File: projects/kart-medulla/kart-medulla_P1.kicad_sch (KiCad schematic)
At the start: 55 parts, among them CN1 1990012, CN10 1990012, CN2 1990012, CN3 1990012, CN4 1990012, CN5 1990012, CN6 1990012, CN7 1990012, CN8 1990012, CN9 1990012, Q3 IRLZ44NPBF, Q4 BSS123_C5184436, U13 MCP4922-E/SL, U14 MAX4660EUA+T, U19 L7805CDT_C20611927, U23 SSW-122-01-T-D, U24 SSW-122-01-T-S, U25 PCF8574T/3,518, U4 LM358DR, U5 SN74LVC3G17DCTR

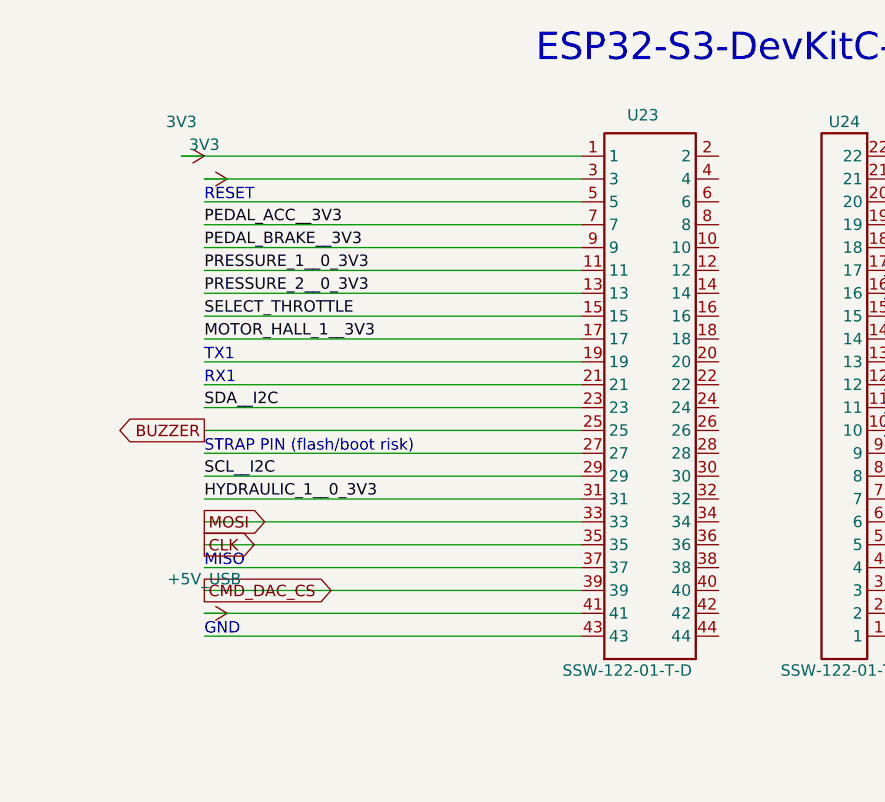
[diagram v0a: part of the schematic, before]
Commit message: kart-medulla: wire ESP32 header pin pairs + add junctions on shared net points
Connect U23 (SSW-122-01-T-D, ESP32 DevKitC double-row header) odd-even
pin pairs 5-6..43-44 horizontally so each row maps to one ESP32 GPIO
visible on both physical rows of the header. Added 22 junction markers
on the left column where label-wires meet the new horizontals (3-way
points need explicit junctions when wires are added programmatically;
KiCad GUI auto-creates them only at draw time). ERC: 111 -> 83.

Co-Authored-By: Claude Opus 4.7 (1M context) <noreply@anthropic.com>
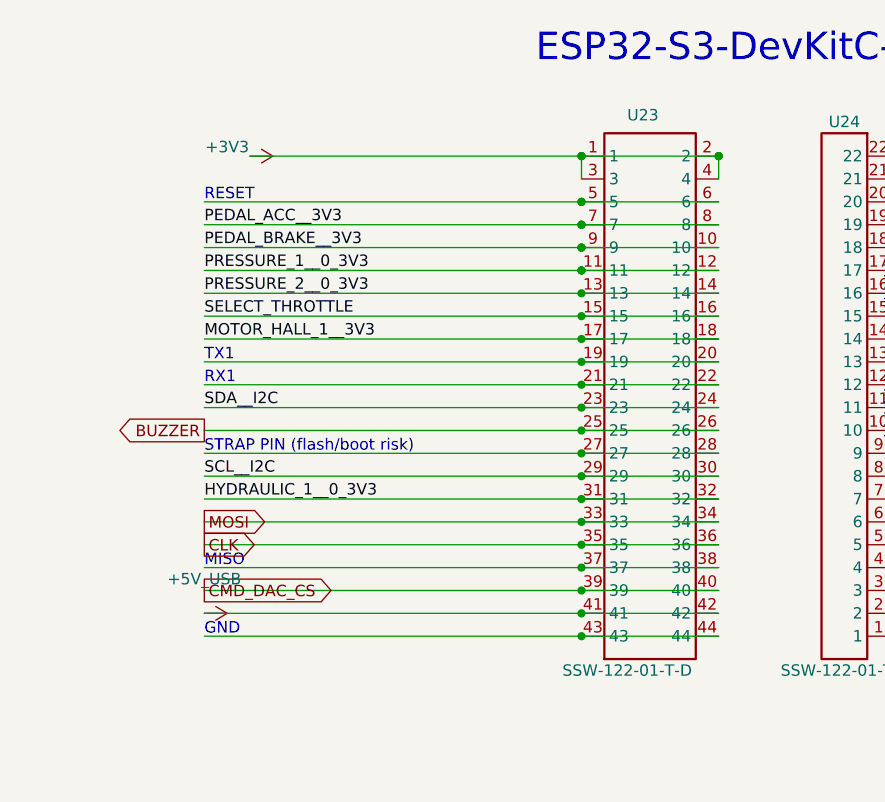
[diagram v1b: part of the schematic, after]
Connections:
- net +5V_USB: now also U23.42
- net 3V3: no longer U23.1, U23.3
- net BUZZER: now also U23.26
- net CLK: now also U23.36
- net CMD_DAC_CS: now also U23.40
- net HYDRAULIC_1__0_3V3: now also U23.32
- net MOSI: now also U23.34
- net MOTOR_HALL_1__3V3: now also U23.18
- net PEDAL_ACC__3V3: now also U23.8
- net PEDAL_BRAKE__3V3: now also U23.10
- net PRESSURE_1__0_3V3: now also U23.12
- net PRESSURE_2__0_3V3: now also U23.14
- net SCL__I2C: now also U23.30
- net SDA__I2C: now also U23.24
- net SELECT_THROTTLE: now also U23.16
- net at U23.19: now also U23.20
- net +3V3: now reaches U23.2
- net +3V3: now also U23.1, U23.3, U23.4
- net at U23.21: now also U23.22
- net at U23.27: now also U23.28
- net at U23.37: now also U23.38
- net at U23.43: now also U23.44
- net at U23.5: now also U23.6

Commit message: kart-medulla: rename power flags to +3V3/+12V; convert U24 text→labels
Two changes:
1. Power flag rename to KiCad stdlib convention: 3V3 → +3V3, 12V → +12V
   (consistent with +5V_REG/+5V_USB which already had +). Touches both
   the project lib and the cached lib_symbols block + all instances.
2. The right-side annotations on U24 ('GND', 'TX0', 'RX0', 'USB_D+/-',
   'LED', 'STRAP_PIN_8', 'SDC_NOT_EMERGENCY__3V3') were plain (text)
   elements — visually labels, but electrically nothing. Replaced with
   real (global_label) at the wire endpoints, snapped to (427.99, y).

ERC: 83 → 70. pin_not_connected on U24: 10 → 0. The remaining
isolated_pin_label warnings on TX0/RX0/USB_D+/-/LED/STRAP_PIN_8 are
legitimate — those signals truly exit the board through one pin each.

Co-Authored-By: Claude Opus 4.7 (1M context) <noreply@anthropic.com>
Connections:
- net 3V3 is gone; now on net +3V3: C1.1, C6.2, CN1.2, R33.2, R34.2, U25.16 (VDD), U5.8 (VCC)
- net GND: now also U24.1, U24.2, U24.22
- net SDC_NOT_EMERGENCY__3V3: now also U24.14
- net RX0: now reaches U24.20
- net TX0: now reaches U24.21
- net USB_D-: now reaches U24.3
- net USB_D+: now reaches U24.4
- net LED: now reaches U24.7
- net STRAP_PIN_8: now reaches U24.8
- net 12V renamed +12V
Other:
- note removed: "LED"
- note removed: "RX0"
- note removed: "SDC_ENABLE"
- note removed: "TX0"
- note removed: "USB_D+"
- note removed: "USB_D-"

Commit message: kart-medulla: convert remaining U23 left-side text→global_labels + fix GND collision
5 more pseudo-labels were plain (text) on the left side of U23
(RESET, TX1, RX1, MISO, GND), each sitting at a wire endpoint but
not electrically connected. Converted to global_label.

Renamed the U24 pin-14 label from SDC_NOT_EMERGENCY__3V3 to
SDC_ENABLE (the actual signal name from the user's original text;
SDC_NOT_EMERGENCY__3V3 is on pin 13 as an existing local label).

Promoted local 'GND' label at (128.27, 78.74) to global to clear the
last same_local_global_label warning. ERC: 70 → 64.

Co-Authored-By: Claude Opus 4.7 (1M context) <noreply@anthropic.com>
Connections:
- net GND: now also U23.43, U23.44
- net SDC_NOT_EMERGENCY__3V3: no longer U24.14
- net TX1: now reaches U23.19, U23.20
- net RX1: now reaches U23.21, U23.22
- net MISO: now reaches U23.37, U23.38
- net RESET: now reaches U23.5, U23.6
- new net SDC_ENABLE: U24.14
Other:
- note removed: "GND"
- note removed: "MISO"
- note removed: "RESET"
- note removed: "RX1"
- note removed: "TX1"
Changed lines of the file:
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@@
 		)
 	)
-	(text "MISO"
-		(exclude_from_sim no)
-		(at 313.69 91.44 0)
-		(effects
-			(font
-				(size 1.27 1.27)
-				(thickness 0.1524)
-			)
-			(justify left bottom)
-		)
-	)
-	(text "SPARE - Octal-PSRAM pin on N8R8"
+		(text "SPARE - Octal-PSRAM pin on N8R8"
 		(exclude_from_sim no)
 		(at 391.16 73.66 0)
@@
 		)
 	)
-	(text "RX1"
-		(exclude_from_sim no)
-		(at 313.69 71.12 0)
-		(effects
-			(font
-				(size 1.27 1.27)
-				(thickness 0.1524)
-			)
-			(justify left bottom)
-		)
-	)
-	(text "Amplify brake 0-5V to 0-10V"
+		(text "Amplify brake 0-5V to 0-10V"
 		(exclude_from_sim no)
 		(at 336.55 281.94 0)
@@
 		)
 	)
-	(text "GND"
-		(exclude_from_sim no)
-		(at 313.69 99.06 0)
-		(effects
-			(font
-				(size 1.27 1.27)
-				(thickness 0.1524)
-			)
-			(justify left bottom)
-		)
-	)
-	(text "STRAP PIN (flash/boot risk)"
+		(text "STRAP PIN (flash/boot risk)"
 		(exclude_from_sim no)
 		(at 313.69 78.74 0)
@@
 		)
 	)
-	(text "TX1"
-		(exclude_from_sim no)
-		(at 313.69 68.58 0)
-		(effects
-			(font
-				(size 1.27 1.27)
-				(thickness 0.1524)
-			)
-			(justify left bottom)
-		)
-	)
-	(text "MAIN CONNECTOR (green push-in)"
+		(text "MAIN CONNECTOR (green push-in)"
 		(exclude_from_sim no)
 		(at 57.15 39.37 0)
@@
 		)
 	)
-	(text "RESET"
-		(exclude_from_sim no)
-		(at 313.69 50.8 0)
-		(effects
-			(font
-				(size 1.27 1.27)
-				(thickness 0.1524)
-			)
-			(justify left bottom)
-		)
-	)
-		(text "Throttle mux\nSend to motor value from sensor by default,\nor esp32 when autonomous"
+			(text "Throttle mux\nSend to motor value from sensor by default,\nor esp32 when autonomous"
 		(exclude_from_sim no)
 		(at 359.41 190.5 0)
@@
 		)
 	)
-	(label "GND"
+	(global_label "GND"
+		(shape input)
 		(at 128.27 78.74 0)
 		(effects
@@
 		)
 	)
-	(global_label "SDC_NOT_EMERGENCY__3V3"
+	(global_label "SDC_ENABLE"
 		(shape input)
 		(at 427.99 66.04 180)
@@
 		(effects
 			(font
+				(size 1.27 1.27)
+			)
+			(justify right)
+		)
+	)
+	(global_label "RESET"
+		(shape input)
+		(at 313.69 50.8 180)
+		(effects
+			(font
+				(size 1.27 1.27)
+			)
+			(justify right)
+		)
+	)
+	(global_label "TX1"
+		(shape input)
+		(at 313.69 68.58 180)
+		(effects
+			(font
+				(size 1.27 1.27)
+			)
+			(justify right)
+		)
+	)
+	(global_label "RX1"
+		(shape input)
+		(at 313.69 71.12 180)
+		(effects
+			(font
+				(size 1.27 1.27)
+			)
+			(justify right)
+		)
+	)
+	(global_label "MISO"
+		(shape input)
+		(at 313.69 91.44 180)
+		(effects
+			(font
+				(size 1.27 1.27)
+			)
+			(justify right)
+		)
+	)
+	(global_label "GND"
+		(shape input)
+		(at 313.69 99.06 180)
+		(effects
+			(font

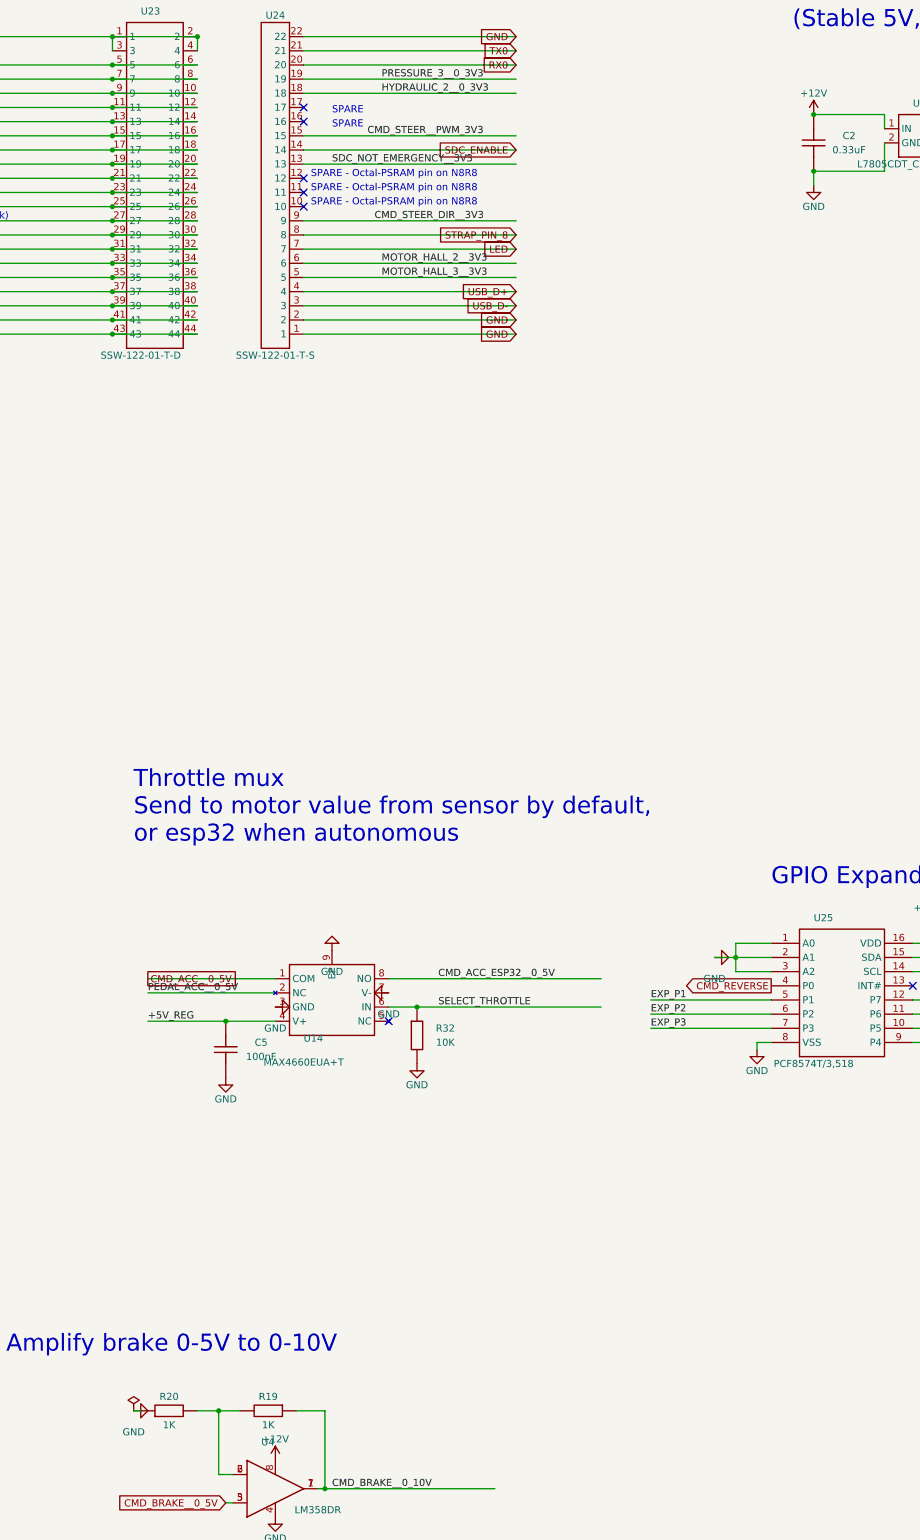
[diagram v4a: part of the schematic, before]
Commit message: kart-medulla: add PWR_FLAG on +12V rail (LM358 amp supply)
Last unflagged power rail. U4 LM358 V+ pin uses +12V for the
0-5V→0-10V brake-amplifier output, but the +12V net had only
power_in consumers. PWR_FLAG asserts the rail is driven from
the main connector. ERC: 61 → 60. All power_pin_not_driven
errors now cleared.

Co-Authored-By: Claude Opus 4.7 (1M context) <noreply@anthropic.com>
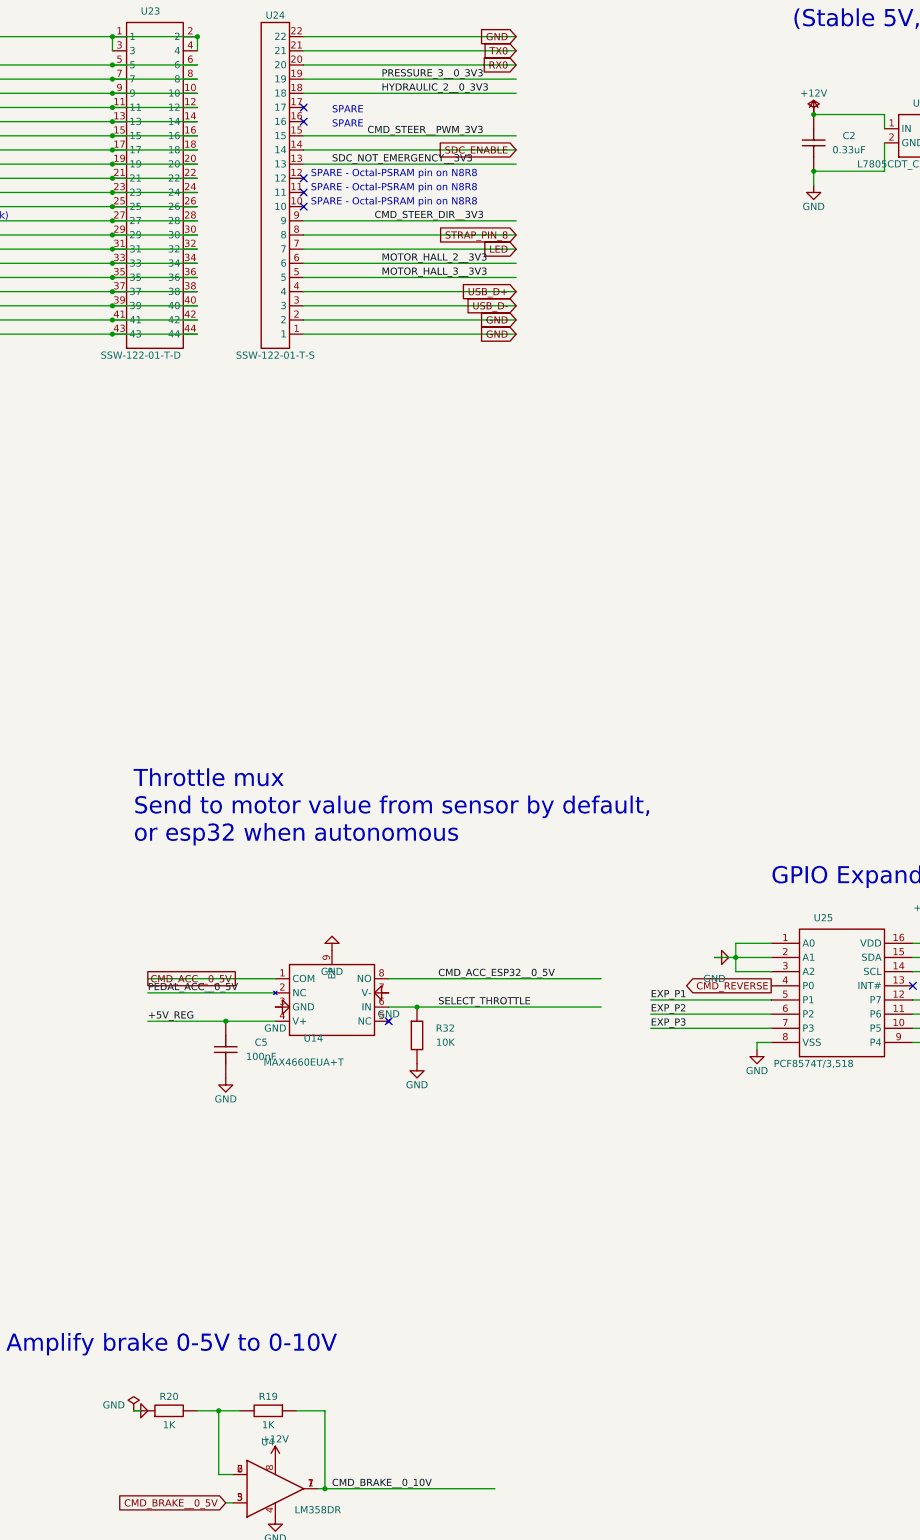
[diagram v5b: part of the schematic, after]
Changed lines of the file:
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@@
 		(in_pos_files yes)
 		(dnp no)
-		(fields_autoplaced yes)
 		(property "Reference" "#PWR08"
 			(at 359.41 294.64 90)
@@
 		)
 		(property "Value" "GND"
-			(at 359.41 295.91 90)
+			(at 355.854 291.084 90)
 			(show_name no)
 			(do_not_autoplace no)
@@
 	)
 	(symbol
+		(lib_id "power:PWR_FLAG")
+		(at 313.69 96.52 0)
+		(unit 1)
+		(body_style 1)
+		(exclude_from_sim no)
+		(in_bom yes)
+		(on_board yes)
+		(in_pos_files yes)
+		(dnp no)
+		(property "Reference" "#FLG_+5V_USB"
+			(at 318.69 94.52 0)
+			(hide yes)
+			(show_name no)
+			(do_not_autoplace no)
+			(effects
+				(font
+					(size 1.27 1.27)
+				)
+			)
+		)
+		(property "Value" "PWR_FLAG"
+			(at 318.69 98.52 0)
+			(hide yes)
+			(show_name no)
+			(do_not_autoplace no)
+			(effects
+				(font
+					(size 1.27 1.27)
+				)
+			)
+		)
+		(property "Footprint" ""
+			(at 313.69 96.52 0)
+			(hide yes)
+			(show_name no)
+			(do_not_autoplace no)
+			(effects
+				(font
+					(size 1.27 1.27)
+				)
+			)
+		)
+		(property "Datasheet" ""
+			(at 313.69 96.52 0)
+			(hide yes)
+			(show_name no)
+			(do_not_autoplace no)
+			(effects
+				(font
+					(size 1.27 1.27)
+				)
+			)
+		)
+		(property "Description" ""
+			(at 313.69 96.52 0)
+			(hide yes)
+			(show_name no)
+			(do_not_autoplace no)
+			(effects
+				(font
+					(size 1.27 1.27)
+				)
+			)
+		)
+		(pin "1"
+		)
+		(instances
+			(project "kart-medulla"
+				(path "/07374be3-c612-51bb-acb6-18bf22cc68ea/ca70726b-7894-594f-a6f9-dfff97cbc924"
+					(reference "#FLG_+5V_USB")
+					(unit 1)
+				)
+			)
+		)
+	)
+	(symbol
 		(lib_id "kart-medulla:Res")
 		(at 516.89 213.36 0)
@@
 	)
 	(symbol
+		(lib_id "power:PWR_FLAG")
+		(at 53.34 49.53 0)
+		(unit 1)
+		(body_style 1)
+		(exclude_from_sim no)
+		(in_bom yes)
+		(on_board yes)
+		(in_pos_files yes)
+		(dnp no)
+		(property "Reference" "#FLG_+3V3"
+			(at 58.34 47.53 0)
+			(hide yes)
+			(show_name no)
+			(do_not_autoplace no)
+			(effects
+				(font
+					(size 1.27 1.27)
+				)
+			)
+		)
+		(property "Value" "PWR_FLAG"
+			(at 58.34 51.53 0)
+			(hide yes)
+			(show_name no)
+			(do_not_autoplace no)
+			(effects
+				(font
+					(size 1.27 1.27)
+				)
+			)
+		)
+		(property "Footprint" ""
+			(at 53.34 49.53 0)
+			(hide yes)
+			(show_name no)
+			(do_not_autoplace no)
+			(effects
+				(font
+					(size 1.27 1.27)
+				)
+			)
+		)
+		(property "Datasheet" ""
+			(at 53.34 49.53 0)
+			(hide yes)
+			(show_name no)
+			(do_not_autoplace no)
+			(effects
+				(font
+					(size 1.27 1.27)
+				)
+			)
+		)
+		(property "Description" ""
+			(at 53.34 49.53 0)
+			(hide yes)
+			(show_name no)
+			(do_not_autoplace no)
+			(effects
+				(font
+					(size 1.27 1.27)
+				)
+			)
+		)
+		(pin "1"
+		)
+		(instances
+			(project "kart-medulla"
+				(path "/07374be3-c612-51bb-acb6-18bf22cc68ea/ca70726b-7894-594f-a6f9-dfff97cbc924"
+					(reference "#FLG_+3V3")
+					(unit 1)
+				)
+			)
+		)
+	)
+	(symbol
 		(lib_id "kart-medulla:Res")
 		(at 83.82 220.98 270)
@@
 	(symbol
 		(lib_id "power:PWR_FLAG")
-		(at 53.34 49.53 0)
+		(at 359.41 292.1 0)
 		(unit 1)
 		(body_style 1)
@@
 		(in_pos_files yes)
 		(dnp no)
-		(property "Reference" "#FLG_+3V3"
-			(at 58.34 47.53 0)
+		(property "Reference" "#FLG_GND"
+			(at 364.41 290.1 0)
+			(hide yes)
 			(show_name no)
 			(do_not_autoplace no)
-			(hide yes)
 			(effects
 				(font
@@
 		)
 		(property "Value" "PWR_FLAG"
-			(at 58.34 51.53 0)
+			(at 364.41 294.1 0)
+			(hide yes)
 			(show_name no)
 			(do_not_autoplace no)
-			(hide yes)
 			(effects
 				(font
@@
 		)
 		(property "Footprint" ""
-			(at 53.34 49.53 0)
-			(show_name no)
-			(do_not_autoplace no)
+			(at 359.41 292.1 0)
 			(hide yes)
-		)
-		(property "Datasheet" ""
-			(at 53.34 49.53 0)
 			(show_name no)
 			(do_not_autoplace no)
-			(hide yes)
-		)
-		(property "Description" ""
-			(at 53.34 49.53 0)
-			(show_name no)
-			(do_not_autoplace no)
-			(hide yes)
-		)
-		(instances
-			(project "kart-medulla"
-				(path "/07374be3-c612-51bb-acb6-18bf22cc68ea/ca70726b-7894-594f-a6f9-dfff97cbc924"
-					(reference "#FLG_+3V3")
-					(unit 1)
+			(effects
+				(font
+					(size 1.27 1.27)
 				)
 			)
 		)
-	)
-	(symbol
-		(lib_id "power:PWR_FLAG")
-		(at 313.69 96.52 0)
-		(unit 1)
-		(body_style 1)
-		(exclude_from_sim no)
-		(in_bom yes)
-		(on_board yes)
-		(in_pos_files yes)
-		(dnp no)
-		(property "Reference" "#FLG_+5V_USB"
-			(at 318.69 94.52 0)
+		(property "Datasheet" ""
+			(at 359.41 292.1 0)
+			(hide yes)
 			(show_name no)
 			(do_not_autoplace no)
-			(hide yes)
 			(effects
 				(font
@@
 			)
 		)
-		(property "Value" "PWR_FLAG"
-			(at 318.69 98.52 0)
+		(property "Description" ""
+			(at 359.41 292.1 0)
+			(hide yes)
 			(show_name no)
 			(do_not_autoplace no)
-			(hide yes)
 			(effects
 				(font
@@
 			)
 		)
-		(property "Footprint" ""
-			(at 313.69 96.52 0)
-			(show_name no)
-			(do_not_autoplace no)
-			(hide yes)
-		)
-		(property "Datasheet" ""
-			(at 313.69 96.52 0)
-			(show_name no)
-			(do_not_autoplace no)
-			(hide yes)
-		)
-		(property "Description" ""
-			(at 313.69 96.52 0)
-			(show_name no)
-			(do_not_autoplace no)
-			(hide yes)
+		(pin "1"
 		)
 		(instances
 			(project "kart-medulla"
 				(path "/07374be3-c612-51bb-acb6-18bf22cc68ea/ca70726b-7894-594f-a6f9-dfff97cbc924"
-					(reference "#FLG_+5V_USB")
+					(reference "#FLG_GND")
 					(unit 1)
 				)
@@
 	(symbol
 		(lib_id "power:PWR_FLAG")
-		(at 359.41 292.1 0)
+		(at 481.33 59.69 0)
 		(unit 1)
 		(body_style 1)
@@
 		(in_pos_files yes)
 		(dnp no)
-		(property "Reference" "#FLG_GND"
-			(at 364.41 290.1 0)
+		(property "Reference" "#FLG_+12V"
+			(at 486.33 57.69 0)
 			(show_name no)
 			(do_not_autoplace no)
@@
 		)
 		(property "Value" "PWR_FLAG"
-			(at 364.41 294.1 0)
+			(at 486.33 61.69 0)
 			(show_name no)
 			(do_not_autoplace no)
@@
 		)
 		(property "Footprint" ""
-			(at 359.41 292.1 0)
+			(at 481.33 59.69 0)
 			(show_name no)
 			(do_not_autoplace no)
@@
 		)
 		(property "Datasheet" ""
-			(at 359.41 292.1 0)
+			(at 481.33 59.69 0)
 			(show_name no)
 			(do_not_autoplace no)
@@
 		)
 		(property "Description" ""
-			(at 359.41 292.1 0)
+			(at 481.33 59.69 0)
 			(show_name no)
 			(do_not_autoplace no)
@@
 			(project "kart-medulla"
 				(path "/07374be3-c612-51bb-acb6-18bf22cc68ea/ca70726b-7894-594f-a6f9-dfff97cbc924"
-					(reference "#FLG_GND")
+					(reference "#FLG_+12V")
 					(unit 1)
 				)
